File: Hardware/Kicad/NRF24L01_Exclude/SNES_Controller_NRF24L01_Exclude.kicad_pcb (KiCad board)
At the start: 2 copper layers, 28 parts, among them J1 Conn_01x07_Socket, J2 Conn_01x08_Socket, Q1 2N7002, Q2 2N7002, Q3 2N7002, SW1 SW_Push, U1 STM32L412KBTx, U2 AMS1117-3.3

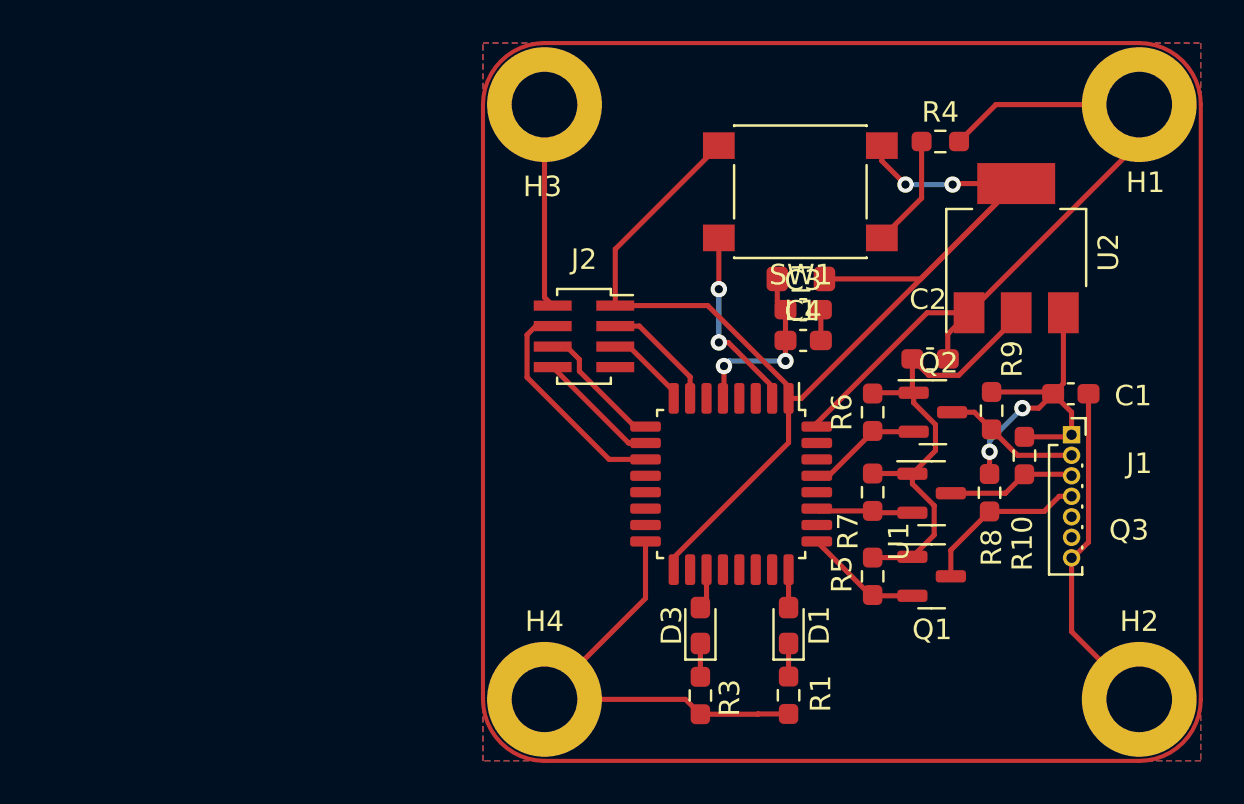
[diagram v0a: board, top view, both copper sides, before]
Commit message: Updated NRF24L01 (Exclude & Include) Kicad projects to revision 2.0
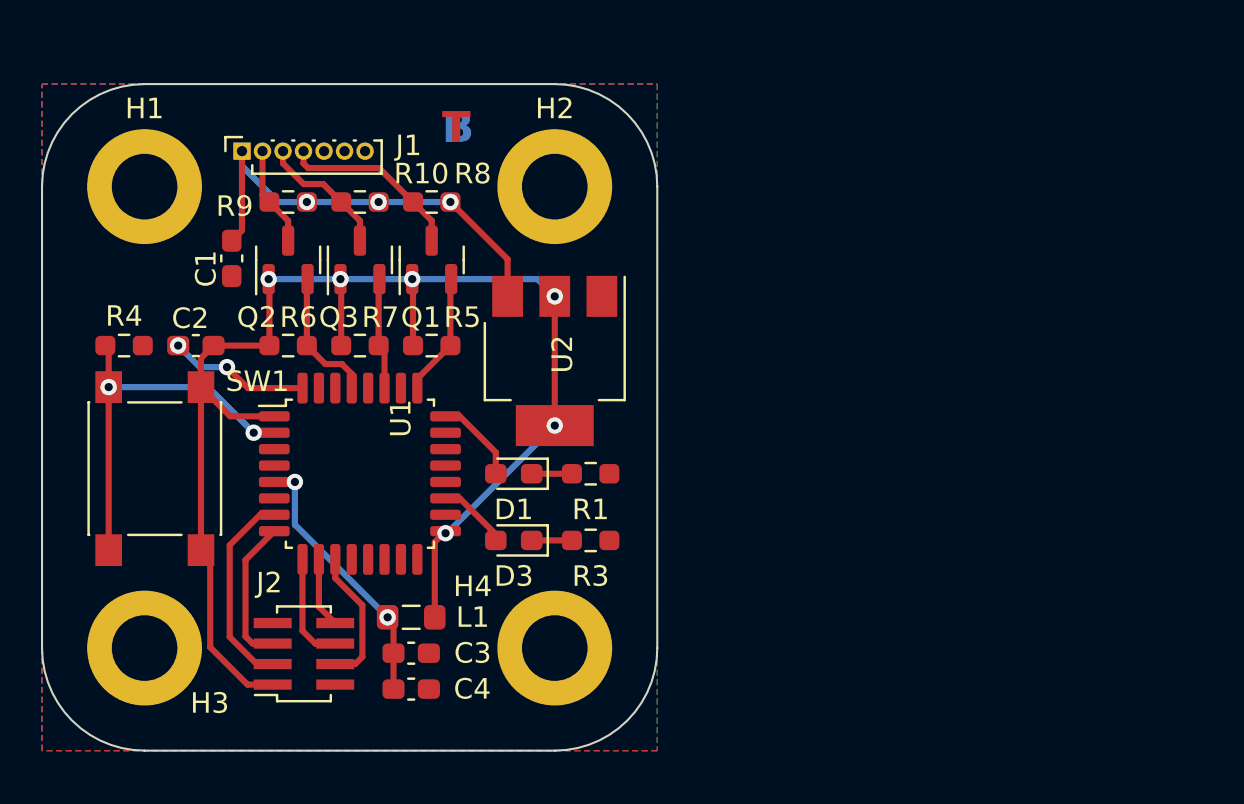
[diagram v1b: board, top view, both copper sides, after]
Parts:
- moved H1 48.7 mm to (124.5, 86.0)
- moved J1 42.7 mm to (129.2, 84.3), turned to 90 degrees
- moved C1 41.4 mm to (128.8, 89.5), turned to -90 degrees
- moved R4 41.0 mm to (123.5, 93.8)
- moved H2 37.9 mm to (144.5, 86.0)
- moved C2 35.8 mm to (127.0, 93.8), turned to 180 degrees
- moved R9 35.8 mm to (131.5, 86.8), turned to 180 degrees
- moved R10 34.7 mm to (135.0, 86.8), turned to 180 degrees
- moved SW1 34.2 mm to (125.0, 99.8), turned to -90 degrees
- moved H3 32.9 mm to (124.5, 108.5)
- moved Q2 32.3 mm to (131.5, 89.6), turned to 90 degrees
- moved R8 30.7 mm to (138.5, 86.8), turned to 180 degrees
- moved Q3 30.1 mm to (135.0, 89.6), turned to 90 degrees
- moved Q1 28.8 mm to (138.5, 89.6), turned to 90 degrees
- moved R6 28.7 mm to (131.5, 93.8), turned to 0 degrees
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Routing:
- net GND: track 86.3 -> 6.92 mm, vias 0 -> 2
- net +3.3V: track 89.9 -> 68.1 mm, vias 2 -> 6
- net +5V: track 17.6 -> 21.9 mm, vias 2 -> 3
- net Appairing_Btn: track 14.7 -> 19.0 mm
- net +3.3VA: track 8.86 -> 13.1 mm
- net SPI_Chip_Select: track 5.73 -> 9.91 mm
- net Chip_Enable: track 10.9 -> 6.77 mm
- net SPI_Digital_Input: track 4.10 -> 7.18 mm
- net SPI_Digital_Output: track 6.06 -> 3.43 mm
- net Player1_LED: track 1.85 -> 4.22 mm
- net Data_Clock_SNES: track 6.69 -> 4.88 mm
- net Status_LED: track 1.97 -> 3.47 mm
- net SPI_Clock: track 6.48 -> 5.34 mm
- net Data_Clock_STM32: track 5.68 -> 6.71 mm
- net Serial_Data_SNES: track 8.25 -> 8.98 mm
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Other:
- board outline added: 30 x 32.5 mm
- board text added: "B"
- board text added: "T"
